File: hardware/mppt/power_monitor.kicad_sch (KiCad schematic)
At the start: 18 parts, among them IC801 INA229AIDGSR

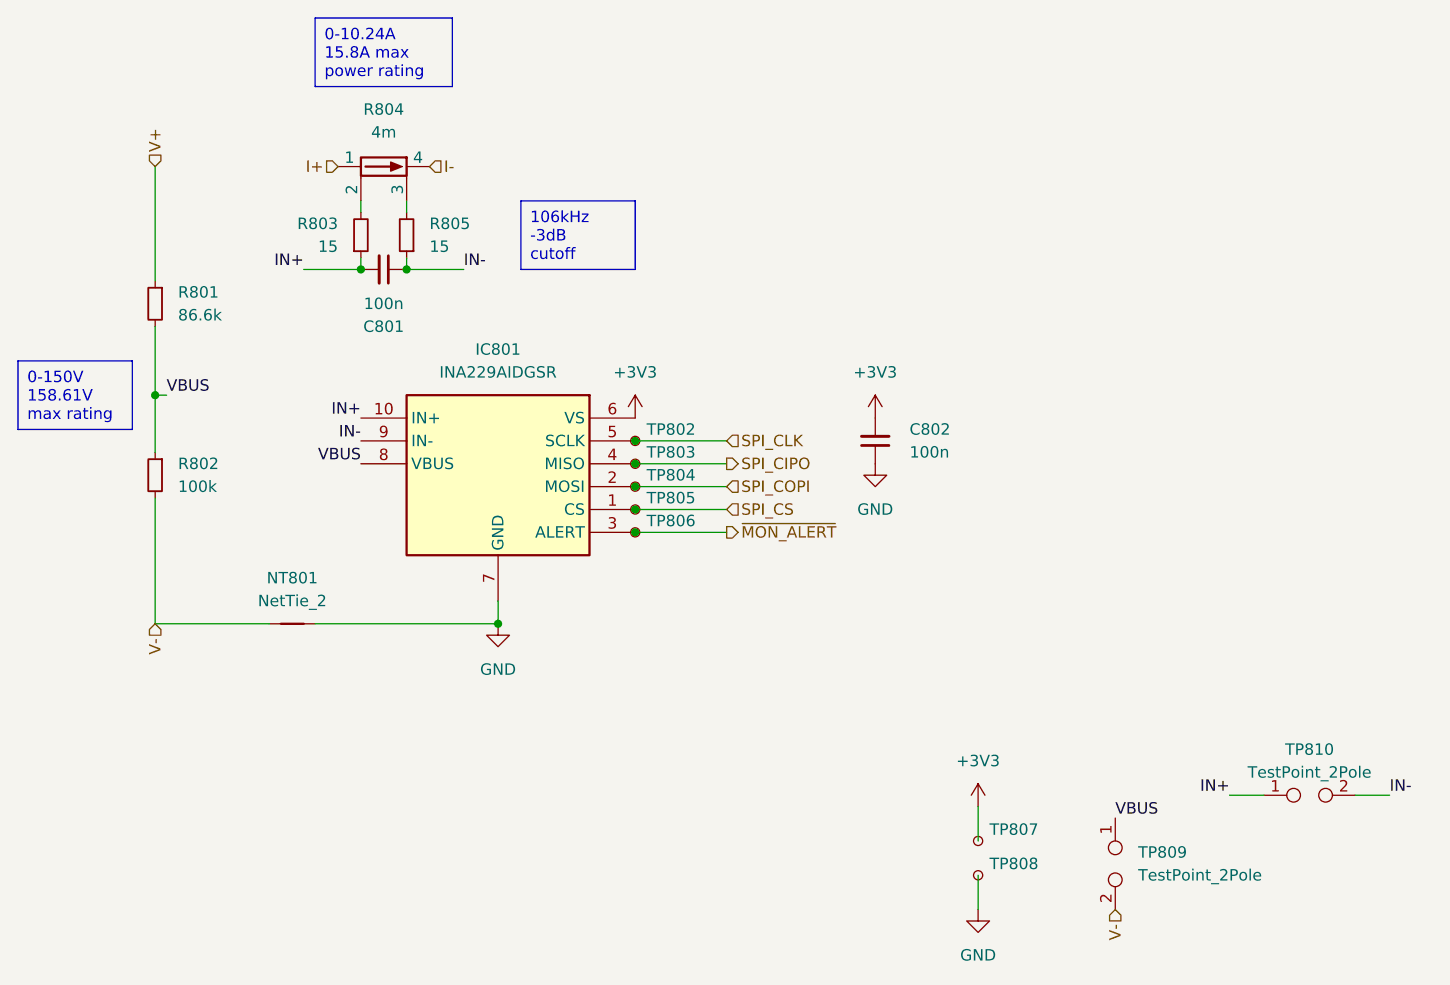
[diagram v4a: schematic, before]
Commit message: PCB variant for power regulation breakout.
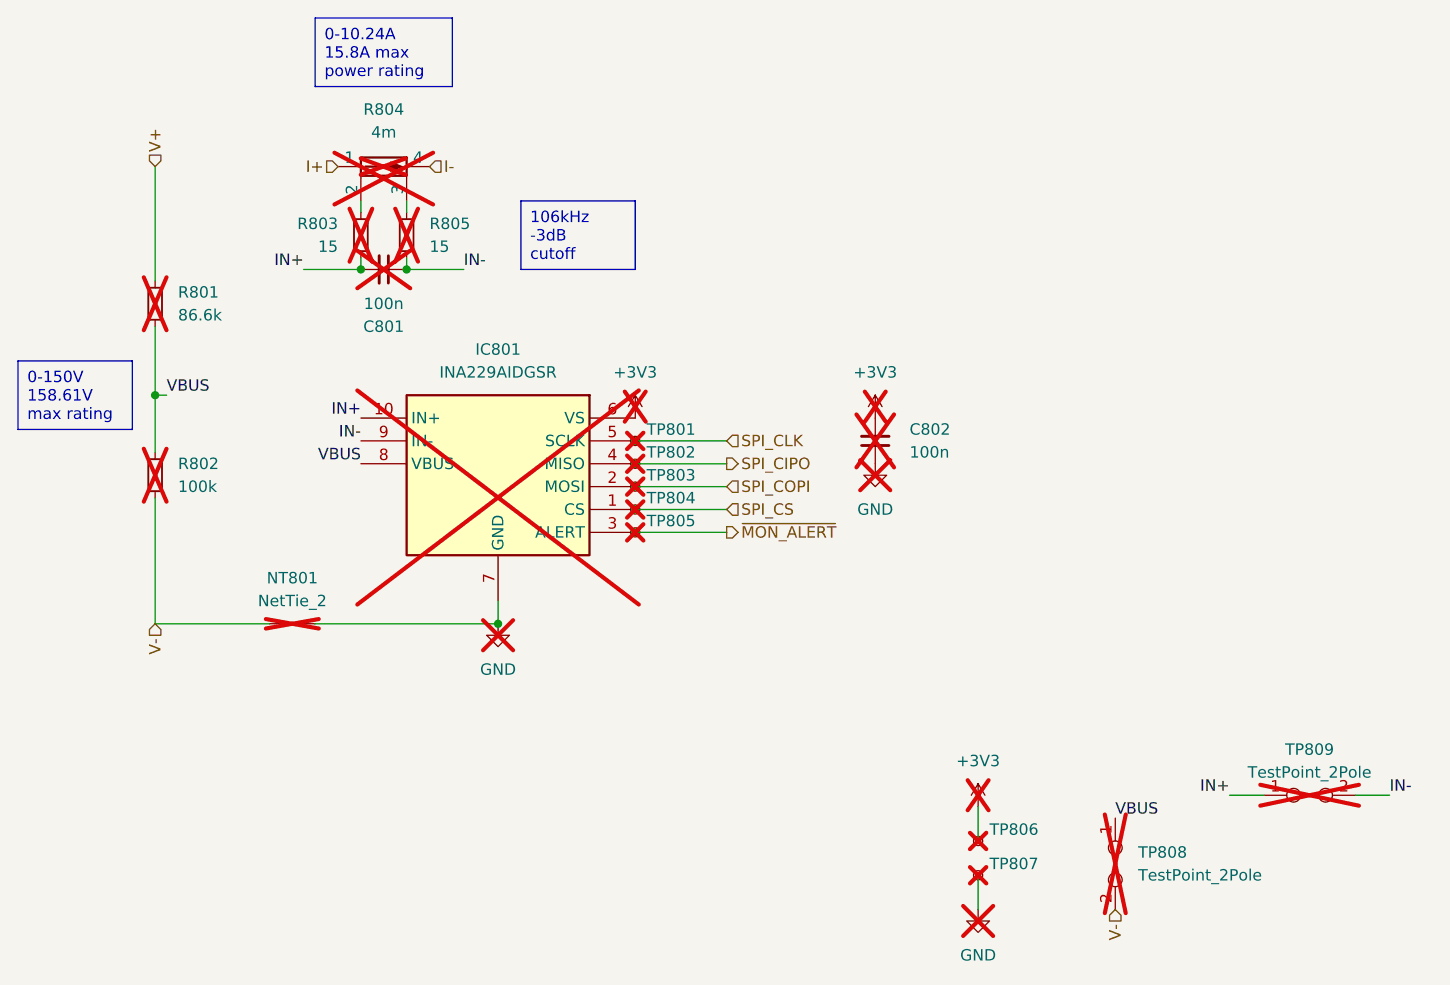
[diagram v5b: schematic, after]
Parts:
- C801, C802, IC801, R801, R802, R803, R804, R805: now not fitted; now left out of the parts list
- NT801: now not fitted; now in the parts list
- TP801: renamed from TP802; now not fitted; now left out of the parts list
- TP802: renamed from TP803; now not fitted; now left out of the parts list
- TP803: renamed from TP804; now not fitted; now left out of the parts list
- TP804: renamed from TP805; now not fitted; now left out of the parts list
- TP805: renamed from TP806; now not fitted; now left out of the parts list
- TP806: renamed from TP807; now not fitted; now left out of the parts list
- TP807: renamed from TP808; now not fitted; now left out of the parts list
- TP808: renamed from TP809; now not fitted; now left out of the parts list
- TP809: renamed from TP810; now not fitted; now left out of the parts list
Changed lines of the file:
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@@
 		(unit 1)
 		(exclude_from_sim no)
-		(in_bom yes)
-		(on_board yes)
-		(dnp no)
+		(in_bom no)
+		(on_board no)
+		(dnp yes)
 		(property "Reference" "C801"
 			(at 114.2937 93.98 90)
@@
 		(unit 1)
 		(exclude_from_sim no)
-		(in_bom yes)
-		(on_board yes)
-		(dnp no)
+		(in_bom no)
+		(on_board no)
+		(dnp yes)
 		(fields_autoplaced yes)
 		(property "Reference" "#PWR0802"
@@
 		(unit 1)
 		(exclude_from_sim no)
-		(in_bom yes)
-		(on_board yes)
-		(dnp no)
+		(in_bom no)
+		(on_board no)
+		(dnp yes)
 		(fields_autoplaced yes)
-		(property "Reference" "TP810"
+		(property "Reference" "TP809"
 			(at 217.17 140.97 0)
 			(effects
@@
 			(project "mppt"
 				(path "/83ad0d2f-976b-4ec4-beba-98e6b6988069/1e7e948a-199f-4420-b7b6-1130e9474bfe/6e1b912f-3d04-4fc7-9635-6a40ec8ca7c8"
-					(reference "TP810")
+					(reference "TP809")
 					(unit 1)
 				)
@@
 		(unit 1)
 		(exclude_from_sim no)
-		(in_bom yes)
-		(on_board yes)
-		(dnp no)
+		(in_bom no)
+		(on_board no)
+		(dnp yes)
 		(fields_autoplaced yes)
 		(property "Reference" "R804"
@@
 		(unit 1)
 		(exclude_from_sim no)
-		(in_bom yes)
-		(on_board yes)
-		(dnp no)
+		(in_bom no)
+		(on_board no)
+		(dnp yes)
 		(property "Reference" "R802"
 			(at 91.44 109.2199 0)
@@
 		(unit 1)
 		(exclude_from_sim no)
-		(in_bom yes)
-		(on_board yes)
-		(dnp no)
+		(in_bom no)
+		(on_board no)
+		(dnp yes)
 		(fields_autoplaced yes)
 		(property "Reference" "#PWR0803"
@@
 		(unit 1)
 		(exclude_from_sim no)
-		(in_bom yes)
-		(on_board yes)
-		(dnp no)
+		(in_bom no)
+		(on_board no)
+		(dnp yes)
 		(fields_autoplaced yes)
 		(property "Reference" "R805"
@@
 		(unit 1)
 		(exclude_from_sim no)
-		(in_bom yes)
-		(on_board yes)
-		(dnp no)
+		(in_bom no)
+		(on_board no)
+		(dnp yes)
 		(fields_autoplaced yes)
-		(property "Reference" "TP805"
+		(property "Reference" "TP804"
 			(at 143.51 113.0299 0)
 			(effects
@@
 			(project "mppt"
 				(path "/83ad0d2f-976b-4ec4-beba-98e6b6988069/1e7e948a-199f-4420-b7b6-1130e9474bfe/6e1b912f-3d04-4fc7-9635-6a40ec8ca7c8"
-					(reference "TP805")
+					(reference "TP804")
 					(unit 1)
 				)
@@
 		(unit 1)
 		(exclude_from_sim no)
-		(in_bom yes)
-		(on_board yes)
-		(dnp no)
+		(in_bom no)
+		(on_board no)
+		(dnp yes)
 		(fields_autoplaced yes)
 		(property "Reference" "IC801"
@@
 		(unit 1)
 		(exclude_from_sim no)
-		(in_bom yes)
-		(on_board yes)
-		(dnp no)
+		(in_bom no)
+		(on_board no)
+		(dnp yes)
 		(property "Reference" "C802"
 			(at 172.72 105.4035 0)
@@
 		(unit 1)
 		(exclude_from_sim no)
-		(in_bom yes)
-		(on_board yes)
-		(dnp no)
+		(in_bom no)
+		(on_board no)
+		(dnp yes)
 		(property "Reference" "R803"
 			(at 109.22 82.5499 0)
@@
 		(unit 1)
 		(exclude_from_sim no)
-		(in_bom yes)
-		(on_board yes)
-		(dnp no)
+		(in_bom no)
+		(on_board no)
+		(dnp yes)
 		(fields_autoplaced yes)
 		(property "Reference" "#PWR0804"
@@
 		(unit 1)
 		(exclude_from_sim no)
-		(in_bom yes)
-		(on_board yes)
-		(dnp no)
+		(in_bom no)
+		(on_board no)
+		(dnp yes)
 		(property "Reference" "R801"
 			(at 91.44 90.1699 0)
@@
 		(unit 1)
 		(exclude_from_sim no)
-		(in_bom yes)
-		(on_board yes)
-		(dnp no)
+		(in_bom no)
+		(on_board no)
+		(dnp yes)
 		(fields_autoplaced yes)
-		(property "Reference" "TP803"
+		(property "Reference" "TP802"
 			(at 143.51 107.9499 0)
 			(effects
@@
 			(project "mppt"
 				(path "/83ad0d2f-976b-4ec4-beba-98e6b6988069/1e7e948a-199f-4420-b7b6-1130e9474bfe/6e1b912f-3d04-4fc7-9635-6a40ec8ca7c8"
-					(reference "TP803")
+					(reference "TP802")
 					(unit 1)
 				)
@@
 		(unit 1)
 		(exclude_from_sim no)
-		(in_bom yes)
-		(on_board yes)
-		(dnp no)
+		(in_bom no)
+		(on_board no)
+		(dnp yes)
 		(fields_autoplaced yes)
-		(property "Reference" "TP807"
+		(property "Reference" "TP806"
 			(at 181.61 149.8599 0)
 			(effects
@@
 			(project "mppt"
 				(path "/83ad0d2f-976b-4ec4-beba-98e6b6988069/1e7e948a-199f-4420-b7b6-1130e9474bfe/6e1b912f-3d04-4fc7-9635-6a40ec8ca7c8"
-					(reference "TP807")
+					(reference "TP806")
 					(unit 1)
 				)
@@
 		(unit 1)
 		(exclude_from_sim no)
-		(in_bom yes)
-		(on_board yes)
-		(dnp no)
+		(in_bom no)
+		(on_board no)
+		(dnp yes)
 		(fields_autoplaced yes)
-		(property "Reference" "TP806"
+		(property "Reference" "TP805"
 			(at 143.51 115.5699 0)
 			(effects
@@
 			(project "mppt"
 				(path "/83ad0d2f-976b-4ec4-beba-98e6b6988069/1e7e948a-199f-4420-b7b6-1130e9474bfe/6e1b912f-3d04-4fc7-9635-6a40ec8ca7c8"
-					(reference "TP806")
+					(reference "TP805")
 					(unit 1)
 				)
@@
 		(unit 1)
 		(exclude_from_sim no)
-		(in_bom yes)
-		(on_board yes)
-		(dnp no)
+		(in_bom no)
+		(on_board no)
+		(dnp yes)
 		(fields_autoplaced yes)
 		(property "Reference" "#PWR0801"
@@
 		(unit 1)
 		(exclude_from_sim no)
-		(in_bom yes)
-		(on_board yes)
-		(dnp no)
+		(in_bom no)
+		(on_board no)
+		(dnp yes)
 		(fields_autoplaced yes)
 		(property "Reference" "#PWR0806"
@@
 		(unit 1)
 		(exclude_from_sim no)
-		(in_bom no)
-		(on_board no)
-		(dnp no)
+		(in_bom yes)
+		(on_board yes)
+		(dnp yes)
 		(fields_autoplaced yes)
 		(property "Reference" "#SYM801"
@@
 		(unit 1)
 		(exclude_from_sim no)
-		(in_bom yes)
-		(on_board yes)
-		(dnp no)
+		(in_bom no)
+		(on_board no)
+		(dnp yes)
 		(fields_autoplaced yes)
-		(property "Reference" "TP802"
+		(property "Reference" "TP801"
 			(at 143.51 105.4099 0)
 			(effects
@@
 			(project "mppt"
 				(path "/83ad0d2f-976b-4ec4-beba-98e6b6988069/1e7e948a-199f-4420-b7b6-1130e9474bfe/6e1b912f-3d04-4fc7-9635-6a40ec8ca7c8"
-					(reference "TP802")
+					(reference "TP801")
 					(unit 1)
 				)
@@
 		(unit 1)
 		(exclude_from_sim no)
-		(in_bom yes)
-		(on_board yes)
-		(dnp no)
+		(in_bom no)
+		(on_board no)
+		(dnp yes)
 		(fields_autoplaced yes)
-		(property "Reference" "TP804"
+		(property "Reference" "TP803"
 			(at 143.51 110.4899 0)
 			(effects
@@
 			(project "mppt"
 				(path "/83ad0d2f-976b-4ec4-beba-98e6b6988069/1e7e948a-199f-4420-b7b6-1130e9474bfe/6e1b912f-3d04-4fc7-9635-6a40ec8ca7c8"
-					(reference "TP804")
+					(reference "TP803")
 					(unit 1)
 				)
@@
 		(unit 1)
 		(exclude_from_sim no)
-		(in_bom yes)
-		(on_board yes)
-		(dnp no)
+		(in_bom no)
+		(on_board no)
+		(dnp yes)
 		(fields_autoplaced yes)
-		(property "Reference" "TP808"
+		(property "Reference" "TP807"
 			(at 181.61 153.6699 0)
 			(effects
@@
 			(project "mppt"
 				(path "/83ad0d2f-976b-4ec4-beba-98e6b6988069/1e7e948a-199f-4420-b7b6-1130e9474bfe/6e1b912f-3d04-4fc7-9635-6a40ec8ca7c8"
-					(reference "TP808")
+					(reference "TP807")
 					(unit 1)
 				)
@@
 		(unit 1)
 		(exclude_from_sim no)
-		(in_bom no)
-		(on_board yes)
-		(dnp no)
+		(in_bom yes)
+		(on_board no)
+		(dnp yes)
 		(fields_autoplaced yes)
 		(property "Reference" "NT801"
@@
 		(unit 1)
 		(exclude_from_sim no)
-		(in_bom yes)
-		(on_board yes)
-		(dnp no)
+		(in_bom no)
+		(on_board no)
+		(dnp yes)
 		(fields_autoplaced yes)
-		(property "Reference" "TP809"
+		(property "Reference" "TP808"
 			(at 198.12 152.3999 90)
 			(effects
@@
 			(project "mppt"
 				(path "/83ad0d2f-976b-4ec4-beba-98e6b6988069/1e7e948a-199f-4420-b7b6-1130e9474bfe/6e1b912f-3d04-4fc7-9635-6a40ec8ca7c8"
-					(reference "TP809")
+					(reference "TP808")
 					(unit 1)
 				)
@@
 		(unit 1)
 		(exclude_from_sim no)
-		(in_bom yes)
-		(on_board yes)
-		(dnp no)
+		(in_bom no)
+		(on_board no)
+		(dnp yes)
 		(fields_autoplaced yes)
 		(property "Reference" "#PWR0805"

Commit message: converter schematic and layout.
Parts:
- C801, C802, IC801, R801, R802, R803, R804, R805, TP801, TP802, TP803, TP804, TP805, TP806, TP807, TP808, TP809: now fitted; now in the parts list
- NT801: now fitted
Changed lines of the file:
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@@
 		(unit 1)
 		(exclude_from_sim no)
-		(in_bom no)
-		(on_board no)
-		(dnp yes)
+		(in_bom yes)
+		(on_board yes)
+		(dnp no)
 		(property "Reference" "C801"
 			(at 114.2937 93.98 90)
@@
 		(unit 1)
 		(exclude_from_sim no)
-		(in_bom no)
-		(on_board no)
-		(dnp yes)
+		(in_bom yes)
+		(on_board yes)
+		(dnp no)
 		(fields_autoplaced yes)
 		(property "Reference" "#PWR0802"
@@
 		(unit 1)
 		(exclude_from_sim no)
-		(in_bom no)
-		(on_board no)
-		(dnp yes)
+		(in_bom yes)
+		(on_board yes)
+		(dnp no)
 		(fields_autoplaced yes)
 		(property "Reference" "TP809"
@@
 		(unit 1)
 		(exclude_from_sim no)
-		(in_bom no)
-		(on_board no)
-		(dnp yes)
+		(in_bom yes)
+		(on_board yes)
+		(dnp no)
 		(fields_autoplaced yes)
 		(property "Reference" "R804"
@@
 		(unit 1)
 		(exclude_from_sim no)
-		(in_bom no)
-		(on_board no)
-		(dnp yes)
+		(in_bom yes)
+		(on_board yes)
+		(dnp no)
 		(property "Reference" "R802"
 			(at 91.44 109.2199 0)
@@
 		(unit 1)
 		(exclude_from_sim no)
-		(in_bom no)
-		(on_board no)
-		(dnp yes)
+		(in_bom yes)
+		(on_board yes)
+		(dnp no)
 		(fields_autoplaced yes)
 		(property "Reference" "#PWR0803"
@@
 		(unit 1)
 		(exclude_from_sim no)
-		(in_bom no)
-		(on_board no)
-		(dnp yes)
+		(in_bom yes)
+		(on_board yes)
+		(dnp no)
 		(fields_autoplaced yes)
 		(property "Reference" "R805"
@@
 		(unit 1)
 		(exclude_from_sim no)
-		(in_bom no)
-		(on_board no)
-		(dnp yes)
+		(in_bom yes)
+		(on_board yes)
+		(dnp no)
 		(fields_autoplaced yes)
 		(property "Reference" "TP804"
@@
 		(unit 1)
 		(exclude_from_sim no)
-		(in_bom no)
-		(on_board no)
-		(dnp yes)
+		(in_bom yes)
+		(on_board yes)
+		(dnp no)
 		(fields_autoplaced yes)
 		(property "Reference" "IC801"
@@
 		(unit 1)
 		(exclude_from_sim no)
-		(in_bom no)
-		(on_board no)
-		(dnp yes)
+		(in_bom yes)
+		(on_board yes)
+		(dnp no)
 		(property "Reference" "C802"
 			(at 172.72 105.4035 0)
@@
 		(unit 1)
 		(exclude_from_sim no)
-		(in_bom no)
-		(on_board no)
-		(dnp yes)
+		(in_bom yes)
+		(on_board yes)
+		(dnp no)
 		(property "Reference" "R803"
 			(at 109.22 82.5499 0)
@@
 		(unit 1)
 		(exclude_from_sim no)
-		(in_bom no)
-		(on_board no)
-		(dnp yes)
+		(in_bom yes)
+		(on_board yes)
+		(dnp no)
 		(fields_autoplaced yes)
 		(property "Reference" "#PWR0804"
@@
 		(unit 1)
 		(exclude_from_sim no)
-		(in_bom no)
-		(on_board no)
-		(dnp yes)
+		(in_bom yes)
+		(on_board yes)
+		(dnp no)
 		(property "Reference" "R801"
 			(at 91.44 90.1699 0)
@@
 		(unit 1)
 		(exclude_from_sim no)
-		(in_bom no)
-		(on_board no)
-		(dnp yes)
+		(in_bom yes)
+		(on_board yes)
+		(dnp no)
 		(fields_autoplaced yes)
 		(property "Reference" "TP802"
@@
 		(unit 1)
 		(exclude_from_sim no)
-		(in_bom no)
-		(on_board no)
-		(dnp yes)
+		(in_bom yes)
+		(on_board yes)
+		(dnp no)
 		(fields_autoplaced yes)
 		(property "Reference" "TP806"
@@
 		(unit 1)
 		(exclude_from_sim no)
-		(in_bom no)
-		(on_board no)
-		(dnp yes)
+		(in_bom yes)
+		(on_board yes)
+		(dnp no)
 		(fields_autoplaced yes)
 		(property "Reference" "TP805"
@@
 		(unit 1)
 		(exclude_from_sim no)
-		(in_bom no)
-		(on_board no)
-		(dnp yes)
+		(in_bom yes)
+		(on_board yes)
+		(dnp no)
 		(fields_autoplaced yes)
 		(property "Reference" "#PWR0801"
@@
 		(unit 1)
 		(exclude_from_sim no)
-		(in_bom no)
-		(on_board no)
-		(dnp yes)
+		(in_bom yes)
+		(on_board yes)
+		(dnp no)
 		(fields_autoplaced yes)
 		(property "Reference" "#PWR0806"
@@
 		(in_bom yes)
 		(on_board yes)
-		(dnp yes)
+		(dnp no)
 		(fields_autoplaced yes)
 		(property "Reference" "#SYM801"
@@
 		(unit 1)
 		(exclude_from_sim no)
-		(in_bom no)
-		(on_board no)
-		(dnp yes)
+		(in_bom yes)
+		(on_board yes)
+		(dnp no)
 		(fields_autoplaced yes)
 		(property "Reference" "TP801"
@@
 		(unit 1)
 		(exclude_from_sim no)
-		(in_bom no)
-		(on_board no)
-		(dnp yes)
+		(in_bom yes)
+		(on_board yes)
+		(dnp no)
 		(fields_autoplaced yes)
 		(property "Reference" "TP803"
@@
 		(unit 1)
 		(exclude_from_sim no)
-		(in_bom no)
-		(on_board no)
-		(dnp yes)
+		(in_bom yes)
+		(on_board yes)
+		(dnp no)
 		(fields_autoplaced yes)
 		(property "Reference" "TP807"
@@
 		(exclude_from_sim no)
 		(in_bom yes)
-		(on_board no)
-		(dnp yes)
+		(on_board yes)
+		(dnp no)
 		(fields_autoplaced yes)
 		(property "Reference" "NT801"
@@
 		(unit 1)
 		(exclude_from_sim no)
-		(in_bom no)
-		(on_board no)
-		(dnp yes)
+		(in_bom yes)
+		(on_board yes)
+		(dnp no)
 		(fields_autoplaced yes)
 		(property "Reference" "TP808"
@@
 		(unit 1)
 		(exclude_from_sim no)
-		(in_bom no)
-		(on_board no)
-		(dnp yes)
+		(in_bom yes)
+		(on_board yes)
+		(dnp no)
 		(fields_autoplaced yes)
 		(property "Reference" "#PWR0805"

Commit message: remove testpoints, integrat 60% of layout
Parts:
- removed TP801, TP802, TP803, TP804, TP805, TP806, TP807: TestPoint_Small, TestPoint:TestPoint_Pad_D1.0mm, symbol Connector:TestPoint_Small
- R803, R805: footprint Resistor_SMD:R_0603_1608Metric_Pad0.98x0.95mm_HandSolder -> Resistor_SMD:R_0603_1608Metric; P/N CRCW060315R0FKEA -> CRCW060315R0FKEAHP
- renumbered TP808 to TP801, TP809 to TP802
